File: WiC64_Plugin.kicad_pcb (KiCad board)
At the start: 2 copper layers, 54.4 x 63.7 mm, 59 parts, among them CN1 USERPORT-C64, CN2 OLED0.96, Q1 BSS138, Q10 BSS138, Q11 BSS138, Q2 BSS138, Q3 BSS138, Q4 BSS138, Q5 BSS138, Q6 BSS138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

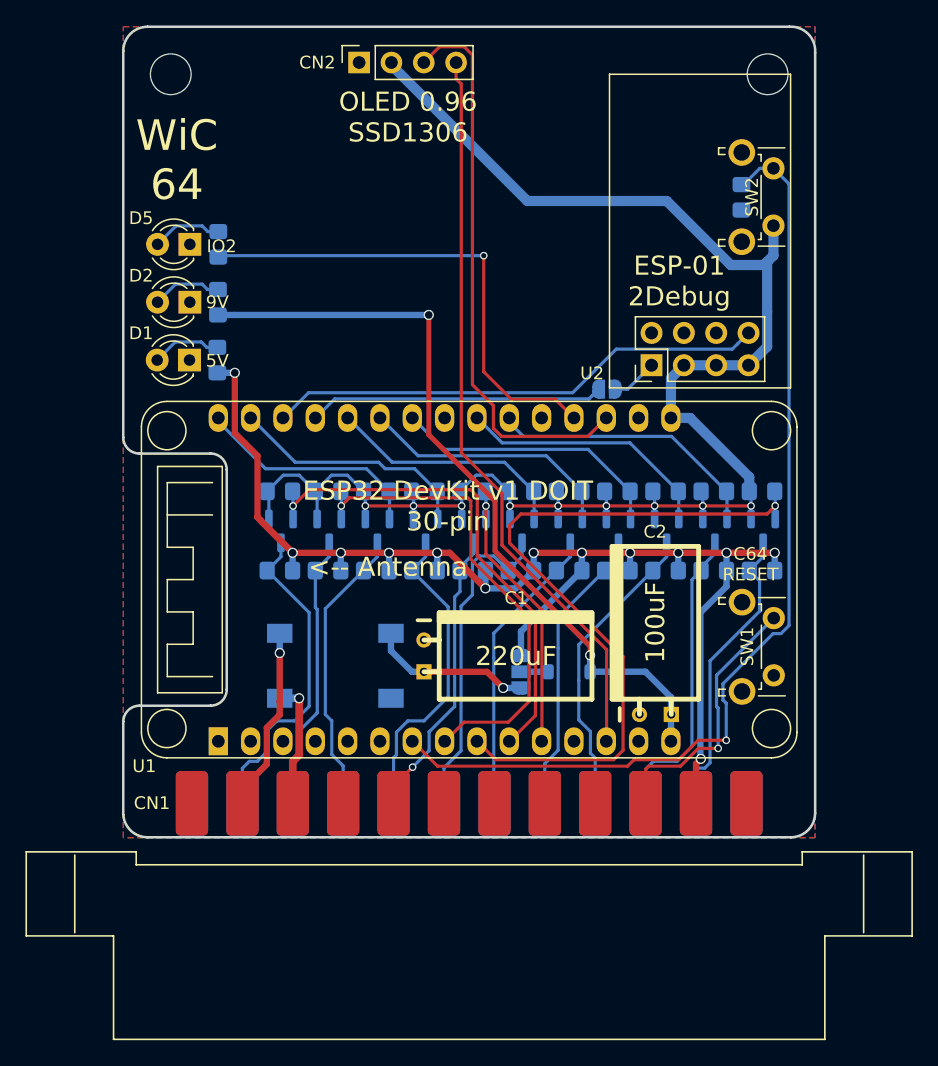
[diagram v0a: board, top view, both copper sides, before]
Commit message: Move all footprints to single library
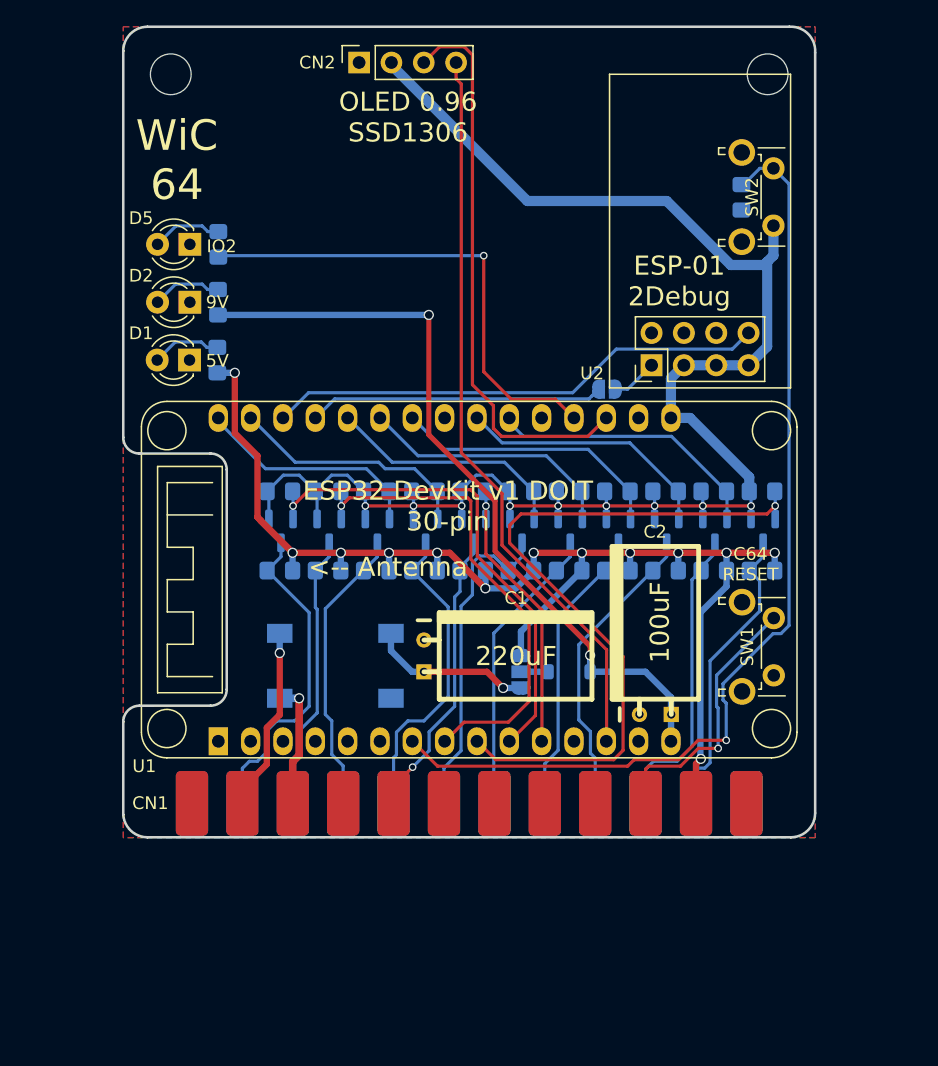
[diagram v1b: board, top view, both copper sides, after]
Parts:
- CN1: footprint cbm-connectors:UPS24CONN -> WiC64:UPS24CONN
- V1: footprint Logo:GMP -> WiC64:GMP
- V2: footprint Logo:YPS2 -> WiC64:YPS2
- V3: footprint Logo:LazyJones2 -> WiC64:LazyJones2
- V4: footprint Logo:KiWi -> WiC64:KiWi
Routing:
- net +3.3V: track 132.3 -> 130.1 mm
- net /PC2: track 22.9 -> 21.5 mm
- net Net-(CN1-9VAC2): track 14.4 -> 13.4 mm

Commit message: Final touches for C64 version
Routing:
- net GND: vias 0 -> 2
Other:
- board text added: "FUNCTION"
- board text added: "Original PCB-Design ©2021 GMP - CC-BY-4.0"
- board text removed: "Original PCB-Design (C) 2021 by GMP"
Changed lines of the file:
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@@
 			(pinfunction "GND1")
 			(pintype "power_in")
-			(solder_mask_margin 0.1016)
 		)
 		(pad "2" smd roundrect
@@
 			(pinfunction "VCC")
 			(pintype "power_out")
-			(solder_mask_margin 0.1016)
 		)
 		(pad "3" smd roundrect
@@
 			(pinfunction "RESET")
 			(pintype "passive")
-			(solder_mask_margin 0.1016)
 		)
 		(pad "4" smd roundrect
@@
 			(pinfunction "CNT")
 			(pintype "input+no_connect")
-			(solder_mask_margin 0.1016)
 		)
 		(pad "5" smd roundrect
@@
 			(pinfunction "SP1")
 			(pintype "bidirectional+no_connect")
-			(solder_mask_margin 0.1016)
 		)
 		(pad "6" smd roundrect
@@
 			(pinfunction "CNT2")
 			(pintype "input+no_connect")
-			(solder_mask_margin 0.1016)
 		)
 		(pad "7" smd roundrect
@@
 			(pinfunction "SP2")
 			(pintype "bidirectional+no_connect")
-			(solder_mask_margin 0.1016)
 		)
 		(pad "8" smd roundrect
@@
 			(pinfunction "PC2")
 			(pintype "output")
-			(solder_mask_margin 0.1016)
 		)
 		(pad "9" smd roundrect
@@
 			(pinfunction "ATN")
 			(pintype "output+no_connect")
-			(solder_mask_margin 0.1016)
 		)
 		(pad "10" smd roundrect
@@
 			(pinfunction "9VAC1")
 			(pintype "power_out")
-			(solder_mask_margin 0.1016)
 		)
 		(pad "11" smd roundrect
@@
 			(pinfunction "9VAC2")
 			(pintype "power_out")
-			(solder_mask_margin 0.1016)
 		)
 		(pad "12" smd roundrect
@@
 			(pinfunction "GND3")
 			(pintype "power_in")
-			(solder_mask_margin 0.1016)
 		)
 		(pad "A" smd roundrect
@@
 			(pinfunction "GND2")
 			(pintype "power_in")
-			(solder_mask_margin 0.1016)
 		)
 		(pad "B" smd roundrect
@@
 			(pinfunction "FLAG2")
 			(pintype "input")
-			(solder_mask_margin 0.1016)
 		)
 		(pad "C" smd roundrect
@@
 			(pinfunction "PB0")
 			(pintype "bidirectional")
-			(solder_mask_margin 0.1016)
 		)
 		(pad "D" smd roundrect
@@
 			(pinfunction "PB1")
 			(pintype "bidirectional")
-			(solder_mask_margin 0.1016)
 		)
 		(pad "E" smd roundrect
@@
 			(pinfunction "PB2")
 			(pintype "bidirectional")
-			(solder_mask_margin 0.1016)
 		)
 		(pad "F" smd roundrect
@@
 			(pinfunction "PB3")
 			(pintype "bidirectional")
-			(solder_mask_margin 0.1016)
 		)
 		(pad "H" smd roundrect
@@
 			(pinfunction "PB4")
 			(pintype "bidirectional")
-			(solder_mask_margin 0.1016)
 		)
 		(pad "J" smd roundrect
@@
 			(pinfunction "PB5")
 			(pintype "bidirectional")
-			(solder_mask_margin 0.1016)
 		)
 		(pad "K" smd roundrect
@@
 			(pinfunction "PB6")
 			(pintype "bidirectional")
-			(solder_mask_margin 0.1016)
 		)
 		(pad "L" smd roundrect
@@
 			(pinfunction "PB7")
 			(pintype "bidirectional")
-			(solder_mask_margin 0.1016)
 		)
 		(pad "M" smd roundrect
@@
 			(pinfunction "PA2")
 			(pintype "bidirectional")
-			(solder_mask_margin 0.1016)
 		)
 		(pad "N" smd roundrect
@@
 			(pinfunction "GND4")
 			(pintype "power_in")
-			(solder_mask_margin 0.1016)
 		)
 		(model "${KIPRJMOD}/3dModels/C64 Userport Connector.step"
@@
 	)
 	(gr_text "5V"
-		(at 152.273 126.1618 0)
+		(at 152.273 126.4158 0)
 		(layer "B.SilkS")
 		(effects
@@
 		)
 	)
-	(gr_text "Original PCB-Design (C) 2021 by GMP"
-		(at 175.0314 108.0389 270)
+	(gr_text "Original PCB-Design ©2021 GMP - CC-BY-4.0"
+		(at 175.26 108.0389 270)
 		(layer "B.SilkS")
 		(effects
@@
 		)
 	)
+	(gr_text "FUNCTION"
+		(at 170.688 84.5058 0)
+		(layer "F.SilkS")
+		(effects
+			(font
+				(size 1 1)
+				(thickness 0.15)
+			)
+			(justify bottom)
+		)
+	)
 	(gr_text "WiC\n64"
 		(at 126.3904 86.6902 0)
@@
 			(extension_offset 0) keep_text_aligned)
 	)
+	(via
+		(at 124.714 137.2108)
+		(size 0.8)
+		(drill 0.6)
+		(layers "F.Cu" "B.Cu")
+		(free yes)
+		(net 1)
+	)
+	(via
+		(at 173.99 137.2108)
+		(size 0.8)
+		(drill 0.6)
+		(layers "F.Cu" "B.Cu")
+		(free yes)
+		(net 1)
+	)
 	(segment
 		(start 135.477 117.5258)
@@
 	)
 	(segment
-		(start 169.545 129.344202)
-		(end 169.545 132.257784)
+		(start 175.006 89.0778)
+		(end 175.006 122.713601)
 		(width 0.25)
 		(layer "B.Cu")
@@
 	)
 	(segment
-		(start 174.478801 123.2408)
-		(end 173.843801 123.8758)
+		(start 170.7388 88.7729)
+		(end 172.1865 87.3252)
 		(width 0.25)
 		(layer "B.Cu")
@@
 	)
 	(segment
-		(start 170.7388 88.7729)
-		(end 172.1865 87.3252)
+		(start 169.291 127.8128)
+		(end 169.291 129.090202)
 		(width 0.25)
 		(layer "B.Cu")
@@
 	)
 	(segment
-		(start 174.478801 88.550601)
-		(end 174.478801 123.2408)
+		(start 175.006 122.713601)
+		(end 173.843801 123.8758)
 		(width 0.25)
 		(layer "B.Cu")
@@
 	)
 	(segment
-		(start 173.843801 123.8758)
-		(end 173.228 123.8758)
+		(start 169.291 129.090202)
+		(end 169.545 129.344202)
 		(width 0.25)
 		(layer "B.Cu")
@@
 	)
 	(segment
-		(start 169.291 127.8128)
-		(end 169.291 129.090202)
+		(start 173.228 123.8758)
+		(end 169.291 127.8128)
 		(width 0.25)
 		(layer "B.Cu")
@@
 	(segment
 		(start 173.2534 87.3252)
-		(end 174.478801 88.550601)
+		(end 175.006 89.0778)
 		(width 0.25)
 		(layer "B.Cu")
@@
 	)
 	(segment
-		(start 169.291 129.090202)
-		(end 169.545 129.344202)
+		(start 169.545 129.344202)
+		(end 169.545 132.257784)
 		(width 0.25)
 		(layer "B.Cu")
@@
 	)
 	(segment
-		(start 172.1865 87.3252)
-		(end 173.2534 87.3252)
+		(start 173.843801 123.8758)
+		(end 173.228 123.8758)
 		(width 0.25)
 		(layer "B.Cu")
@@
 	)
 	(segment
-		(start 173.228 123.8758)
-		(end 169.291 127.8128)
+		(start 172.1865 87.3252)
+		(end 173.2534 87.3252)
 		(width 0.25)
 		(layer "B.Cu")
@@
 			)
 		)
+	)
+	(zone
+		(net 0)
+		(net_name "")
+		(layers "F&B.Cu")
+		(hatch edge 0.5)
+		(connect_pads
+			(clearance 0)
+		)
+		(min_thickness 0.25)
+		(filled_areas_thickness no)
+		(keepout
+			(tracks allowed)
+			(vias allowed)
+			(pads allowed)
+			(copperpour not_allowed)
+			(footprints allowed)
+		)
+		(fill
+			(thermal_gap 0.5)
+			(thermal_bridge_width 0.5)
+		)
+		(polygon
+			(pts
+				(xy 128.397 134.4168) (xy 128.397 139.8778) (xy 170.434 139.8778) (xy 170.434 134.4168)
+			)
+		)

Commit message: WIP
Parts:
- removed JP2: JMP_ESP_POWER, Jumper:SolderJumper-3_P1.3mm_Open_RoundedPad1.0x1.5mm
- added D2: 1N5819, Diode_SMD:D_SMA, B.Cu at (151.7, 123.7)
- added FB1: FERRITE, WiC64:Ferrite_D6.0mm_L10.00mm_Horizontal, F.Cu at (163.7, 126.4)
- C1: footprint w_capacitors:CP_6.3x11mm_horiz-R -> WiC64:CP_6.3x11mm_horiz-R
- C2: value 100uF -> 220uF; footprint w_capacitors:CP_6.3x11mm_horiz-R -> WiC64:CP_6.3x11mm_horiz-R
- D3: footprint Diode_SMD:D_SOD-123 -> Diode_SMD:D_SMA
- moved C2 5.46 mm to (158.9, 128.2)
- moved D3 1.71 mm to (158.4, 125.7)
- moved C1 0.50 mm to (146.2, 125.3), turned to 180 degrees
- moved D1 0.30 mm to (138.8, 126.1)
- renumbered D4 to D1, D1 to LD1, D2 to LD2, D5 to LD3
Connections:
- C1 pad 1: Net-(D4-+) -> Net-(D1-+)
- CN1 pad 2: +5V -> Net-(CN1-VCC)
- D1 pad 1: Net-(D4-+) -> Net-(D1-+)
- D3 pad 2: Net-(D3-A) -> Net-(D1-+)
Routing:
- net Net-(D4-+): track 12.8 -> 0.00 mm, vias 1 -> 0
- net Net-(D1-+): track 0.00 -> 8.61 mm
- net +5V: track 104.1 -> 98.6 mm
- net VCC: track 60.5 -> 57.0 mm
- net /PB0: track 23.6 -> 26.9 mm
- net Net-(D3-A): track 2.13 -> 0.00 mm

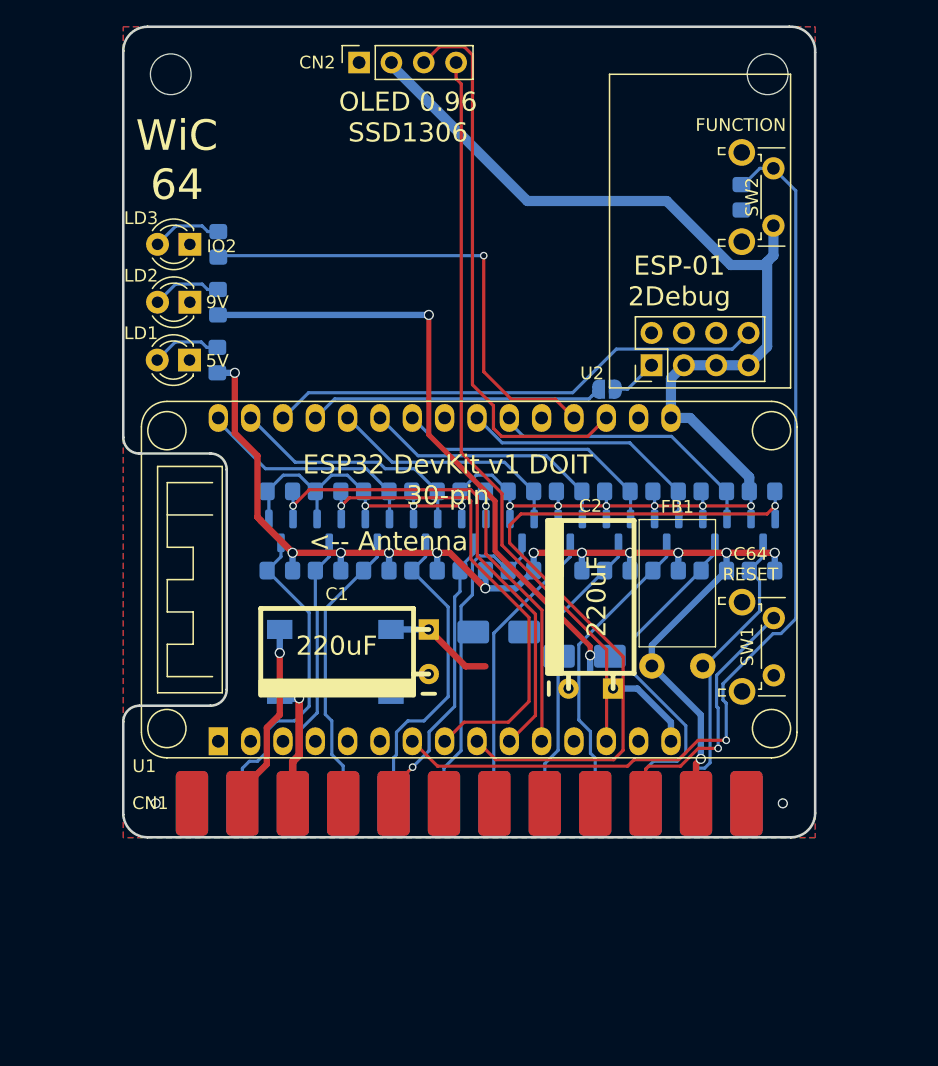
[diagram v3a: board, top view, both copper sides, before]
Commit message: Add diode so that power source is selected automatically
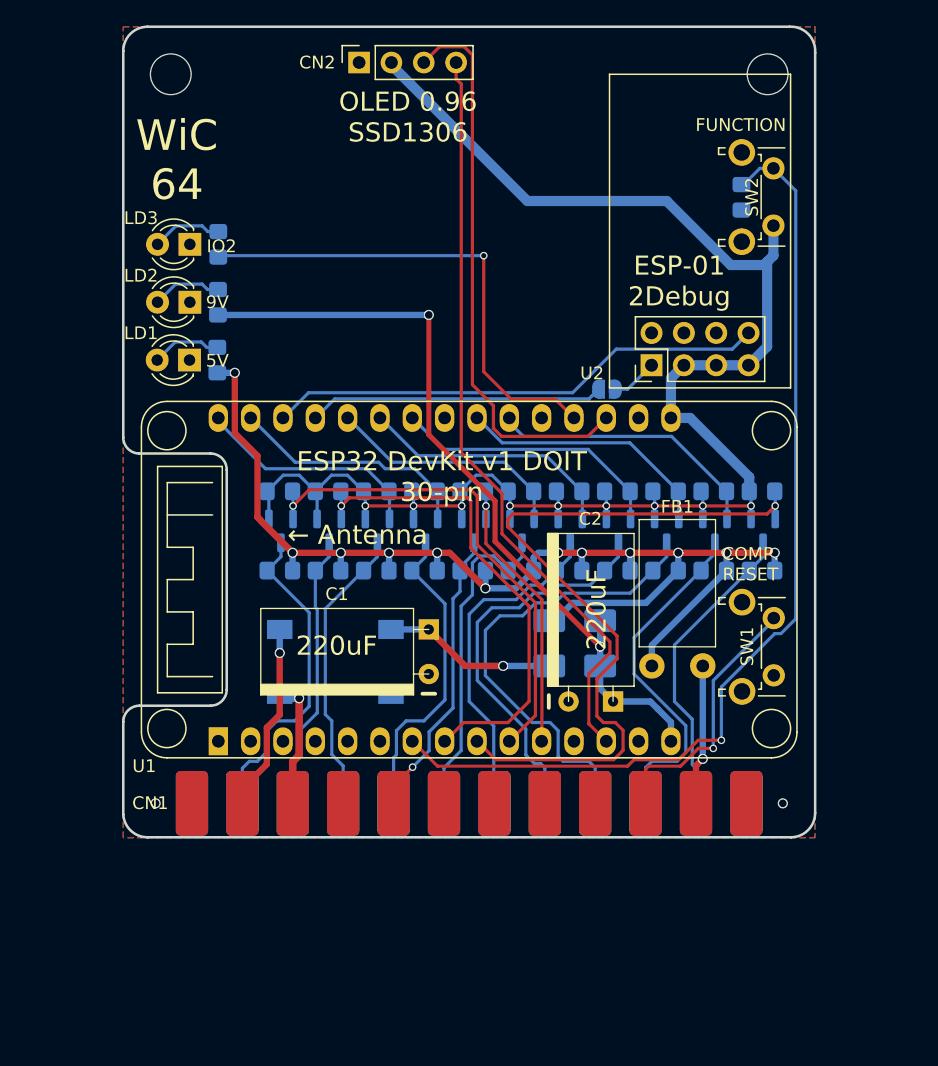
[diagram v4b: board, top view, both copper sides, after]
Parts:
- moved V3 29.9 mm to (153.2, 96.7)
- moved D2 6.03 mm to (157.6, 122.9)
- moved V1 2.37 mm to (141.0, 94.4)
- moved V2 2.15 mm to (164.1, 93.4)
- moved D3 1.08 mm to (157.6, 126.4)
- moved C2 1.02 mm to (158.9, 129.2)
- moved V4 0.28 mm to (166.9, 126.5)
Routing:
- net /PB1: track 23.9 -> 36.9 mm
- net Net-(CN1-VCC): track 0.00 -> 11.0 mm, vias 0 -> 1
- net /PB2: track 22.7 -> 30.8 mm
- net Net-(D1-+): track 8.61 -> 13.6 mm, vias 0 -> 1
- net VCC: track 57.0 -> 61.7 mm
- net /PB3: track 22.7 -> 26.3 mm
- net /IO26: track 57.4 -> 59.7 mm
- net /SDA: track 58.2 -> 59.6 mm
- net +5V: track 98.6 -> 97.8 mm, vias 13 -> 12
- net /SW2C: track 77.9 -> 77.4 mm
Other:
- board text added: "COMP. RESET"
- board text added: "← Antenna"
- board text removed: "5V"
- board text removed: "9V"
- board text removed: "<-- Antenna"
- board text removed: "C64 RESET"

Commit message: Add Pear logo + Connect 9V power led to actual 9V
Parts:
- added V6: SukkoPera, WiC64:PearLogo, B.Cu at (130.2, 82.9)
- LD3: value IO2 -> ACT
- moved V3 2.69 mm to (154.1, 94.2)
- moved V1 1.44 mm to (142.0, 95.4)
- moved V2 0.64 mm to (164.5, 93.9)
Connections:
- C1 pad 1: Net-(D1-+) -> +9V
- D1 pad 1: Net-(D1-+) -> +9V
- D3 pad 2: Net-(D1-+) -> +9V
- R24 pad 1: VCC -> +9V
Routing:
- net +9V: track 0.00 -> 61.7 mm, vias 0 -> 3
- net VCC: track 61.7 -> 13.5 mm, vias 2 -> 0
- net Net-(D1-+): track 13.6 -> 0.00 mm, vias 1 -> 0
- net /IO26: track 59.7 -> 61.0 mm
- net /SDA: track 59.6 -> 60.8 mm
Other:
- board text added: "Rev. 0.7-Sukko"
- board text added: "SukkoPera"
- board text added: "The C64/+4 Wireless Interface Card"
- board text removed: "Rev. 0.6-Sukko"
- board text removed: "The Commodore 64 Wireless Interface Card"
